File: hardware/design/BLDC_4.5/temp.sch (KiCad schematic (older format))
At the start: 2 parts

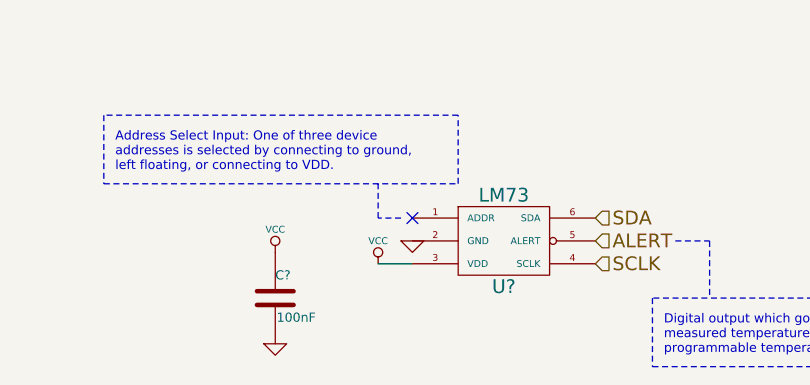
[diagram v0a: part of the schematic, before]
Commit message: Schematic changes: Cleaner top level, added CAN connector, moved LEDs to top level, added 22 Ohm resistors for the USB lines. Fully annotated schematic, ready for layout.
Signed-off-by: Marcos Chaparro <marcos@mrkindustries.com.ar>
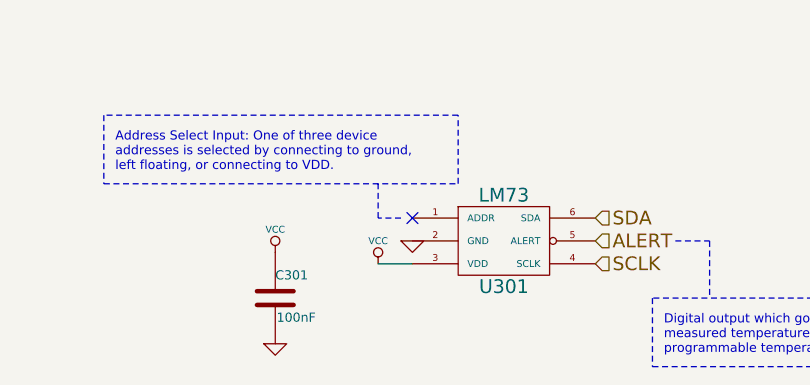
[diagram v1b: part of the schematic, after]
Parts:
- gave numbers to parts that had none: 2
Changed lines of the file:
@@
 LIBS:valves
 LIBS:mrk-industries
+LIBS:crf_1
 LIBS:BLDC_4-cache
 EELAYER 24 0
@@
 $Descr A4 11693 8268
 encoding utf-8
-Sheet 5 6
-Title ""
-Date ""
+Sheet 3 7
+Title "I²C digital temperature sensor"
+Date "25 Aug 2014"
 Rev ""
-Comp ""
+Comp "Mrk Industries"
 Comment1 ""
 Comment2 ""
@@
 $EndDescr
 $Comp
-L LM73 U?
+L LM73 U301
 U 1 1 53F5A7D3
 P 5800 3400
-F 0 "U?" H 5800 3200 60  0000 C CNN
+F 0 "U301" H 5800 3200 60  0000 C CNN
 F 1 "LM73" H 5800 3600 60  0000 C CNN
 F 2 "SMD_Packages:SOT-23-6" H 5800 3150 60  0001 C CNN
@@
 $EndComp
 $Comp
-L GND #PWR?
+L GND #PWR304
 U 1 1 53F5A7F7
 P 5400 3400
-F 0 "#PWR?" H 5400 3400 30  0001 C CNN
+F 0 "#PWR304" H 5400 3400 30  0001 C CNN
 F 1 "GND" H 5400 3330 30  0001 C CNN
 F 2 "" H 5400 3400 60  0000 C CNN
@@
 $EndComp
 $Comp
-L VCC #PWR?
+L VCC #PWR303
 U 1 1 53F5AB35
 P 5250 3500
-F 0 "#PWR?" H 5250 3600 30  0001 C CNN
+F 0 "#PWR303" H 5250 3600 30  0001 C CNN
 F 1 "VCC" H 5250 3600 30  0000 C CNN
 F 2 "" H 5250 3500 60  0001 C CNN
@@
 NoConn ~ 5400 3300
 $Comp
-L C C?
+L C C301
 U 1 1 53F5AB44
 P 4800 3650
-F 0 "C?" H 4800 3750 40  0000 L CNN
+F 0 "C301" H 4800 3750 40  0000 L CNN
 F 1 "100nF" H 4806 3565 40  0000 L CNN
 F 2 "" H 4838 3500 30  0000 C CNN
@@
 $EndComp
 $Comp
-L VCC #PWR?
+L VCC #PWR301
 U 1 1 53F5AB73
 P 4800 3450
-F 0 "#PWR?" H 4800 3550 30  0001 C CNN
+F 0 "#PWR301" H 4800 3550 30  0001 C CNN
 F 1 "VCC" H 4800 3550 30  0000 C CNN
 F 2 "" H 4800 3450 60  0001 C CNN
@@
 $EndComp
 $Comp
-L GND #PWR?
+L GND #PWR302
 U 1 1 53F5AB80
 P 4800 3850
-F 0 "#PWR?" H 4800 3850 30  0001 C CNN
+F 0 "#PWR302" H 4800 3850 30  0001 C CNN
 F 1 "GND" H 4800 3780 30  0001 C CNN
 F 2 "" H 4800 3850 60  0000 C CNN
@@
 41 E2 CF 04 72 F7 8E 04 09 12 24 48 90 20 41 E2 CF 09 D2 CF 23 41 82 04 09 12 24 48 90 F8 73 82
 F4 F3 48 90 20 41 82 04 09 12 24 FE 9C 20 FD 3C 12 24 48 90 20 41 82 04 89 3F 27 FE 1F 21 12 69
-2F 52 6F B5 AD 00 00 00 00 49 45 4E 44 AE 42 60 82 B0
+2F 52 6F B5 AD 00 00 00 00 49 45 4E 44 AE 42 60 82 46
 EndData
 $EndBitmap

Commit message: Layout updated. Added inner power planes, changed USB connector, added CAN transceiver and connector, added 3D models copper pour under the mosfets and references moved to visible places
Signed-off-by: Marcos Chaparro <marcos@mrkindustries.com.ar>
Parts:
- C301: footprint (none) -> SMD_Packages:SMD-0603
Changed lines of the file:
@@
 $EndComp
 $Comp
-L GND #PWR304
+L GND #PWR024
 U 1 1 53F5A7F7
 P 5400 3400
-F 0 "#PWR304" H 5400 3400 30  0001 C CNN
+F 0 "#PWR024" H 5400 3400 30  0001 C CNN
 F 1 "GND" H 5400 3330 30  0001 C CNN
 F 2 "" H 5400 3400 60  0000 C CNN
@@
 $EndComp
 $Comp
-L VCC #PWR303
+L VCC #PWR025
 U 1 1 53F5AB35
 P 5250 3500
-F 0 "#PWR303" H 5250 3600 30  0001 C CNN
+F 0 "#PWR025" H 5250 3600 30  0001 C CNN
 F 1 "VCC" H 5250 3600 30  0000 C CNN
 F 2 "" H 5250 3500 60  0001 C CNN
@@
 F 0 "C301" H 4800 3750 40  0000 L CNN
 F 1 "100nF" H 4806 3565 40  0000 L CNN
-F 2 "" H 4838 3500 30  0000 C CNN
+F 2 "SMD_Packages:SMD-0603" H 4838 3500 30  0001 C CNN
 F 3 "" H 4800 3650 60  0000 C CNN
 	1    4800 3650
@@
 $EndComp
 $Comp
-L VCC #PWR301
+L VCC #PWR026
 U 1 1 53F5AB73
 P 4800 3450
-F 0 "#PWR301" H 4800 3550 30  0001 C CNN
+F 0 "#PWR026" H 4800 3550 30  0001 C CNN
 F 1 "VCC" H 4800 3550 30  0000 C CNN
 F 2 "" H 4800 3450 60  0001 C CNN
@@
 $EndComp
 $Comp
-L GND #PWR302
+L GND #PWR027
 U 1 1 53F5AB80
 P 4800 3850
-F 0 "#PWR302" H 4800 3850 30  0001 C CNN
+F 0 "#PWR027" H 4800 3850 30  0001 C CNN
 F 1 "GND" H 4800 3780 30  0001 C CNN
 F 2 "" H 4800 3850 60  0000 C CNN
@@
 $Bitmap
 Pos 5600 4800
-Scale 1.000000
+Scale 1,000000
 Data
 89 50 4E 47 0D 0A 1A 0A 00 00 00 0D 49 48 44 52 00 00 02 6B 00 00 01 29 08 02 00 00 00 43 56 F2
@@
 $Bitmap
 Pos 3100 4000
-Scale 1.000000
+Scale 1,000000
 Data
 89 50 4E 47 0D 0A 1A 0A 00 00 00 0D 49 48 44 52 00 00 02 F0 00 00 01 AA 08 02 00 00 00 E2 39 E7
@@
 $Bitmap
 Pos 3200 5300
-Scale 1.000000
+Scale 1,000000
 Data
 89 50 4E 47 0D 0A 1A 0A 00 00 00 0D 49 48 44 52 00 00 03 4D 00 00 00 CE 08 02 00 00 00 6D AD 7E
@@
 41 E2 CF 04 72 F7 8E 04 09 12 24 48 90 20 41 E2 CF 09 D2 CF 23 41 82 04 09 12 24 48 90 F8 73 82
 F4 F3 48 90 20 41 82 04 09 12 24 FE 9C 20 FD 3C 12 24 48 90 20 41 82 04 89 3F 27 FE 1F 21 12 69
-2F 52 6F B5 AD 00 00 00 00 49 45 4E 44 AE 42 60 82 46
+2F 52 6F B5 AD 00 00 00 00 49 45 4E 44 AE 42 60 82 00
 EndData
 $EndBitmap
 $Bitmap
 Pos 7150 4850
-Scale 1.000000
+Scale 1,000000
 Data
 89 50 4E 47 0D 0A 1A 0A 00 00 00 0D 49 48 44 52 00 00 00 C8 00 00 00 C8 08 02 00 00 00 22 3A 39
